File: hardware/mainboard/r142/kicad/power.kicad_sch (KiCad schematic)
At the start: 44 parts, among them J1 1S LiPo PCM / PH-2, J8 External cell NTC / hand sold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, Q2 AO3401A, SW1 MK-12C03-G015, U3 BQ24072TRGTR, U4 TPS63802DLAR

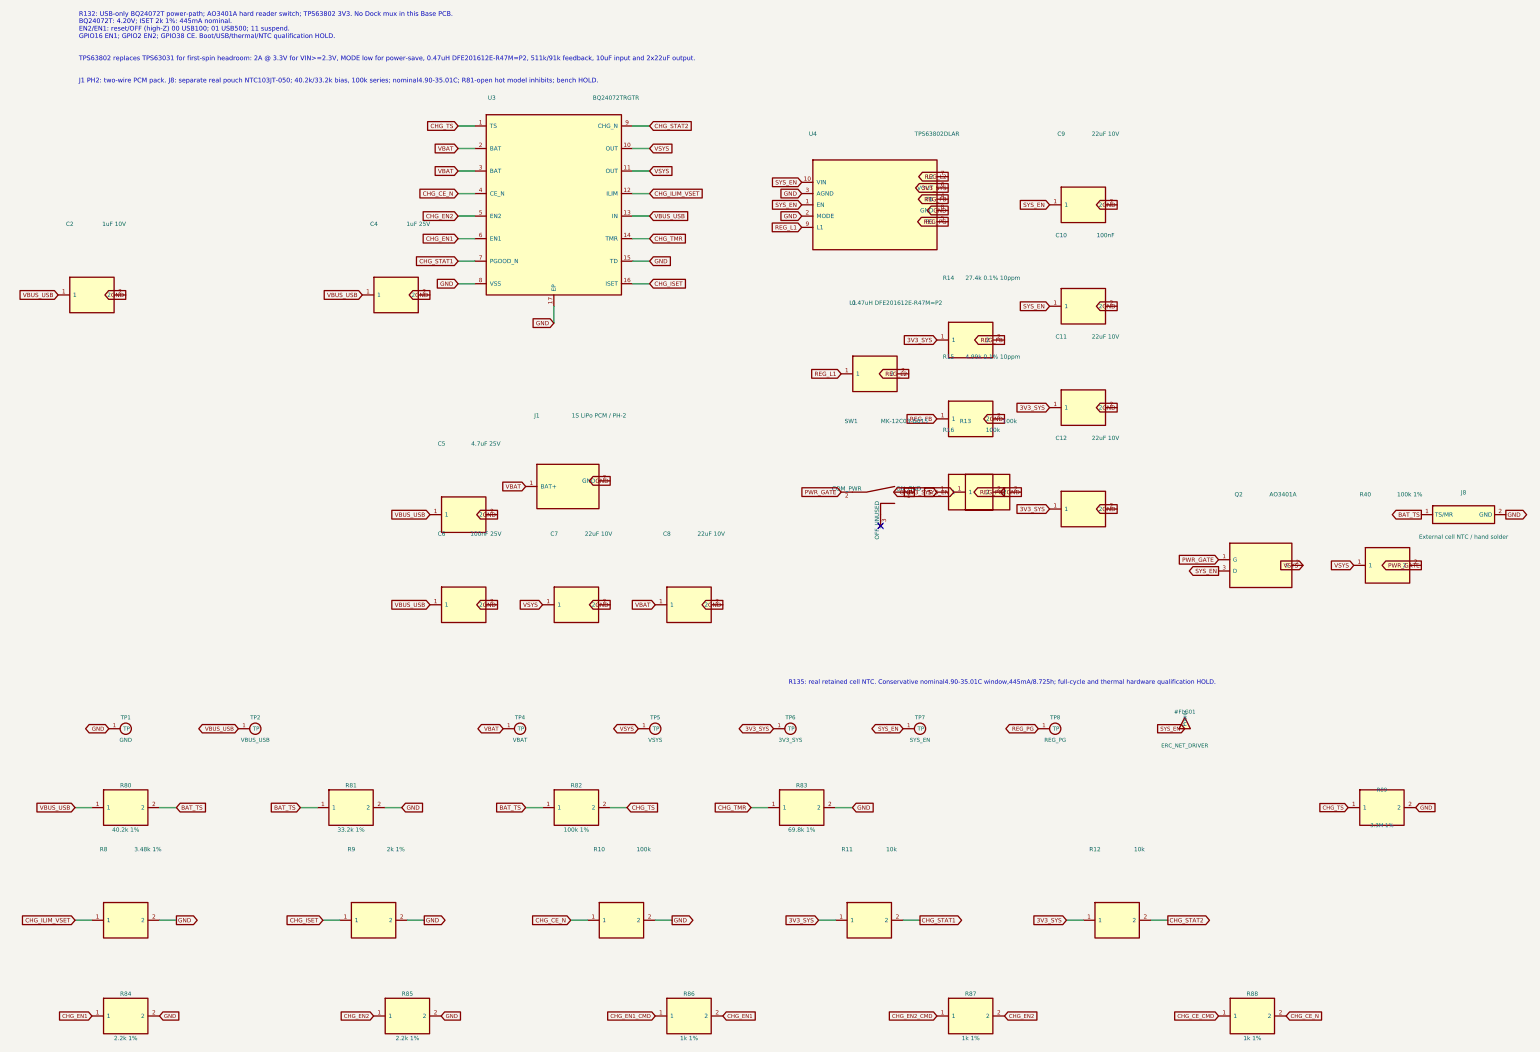
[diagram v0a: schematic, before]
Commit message: R142: separate SD schematic group and refresh engineering notes; preserve electrical graph
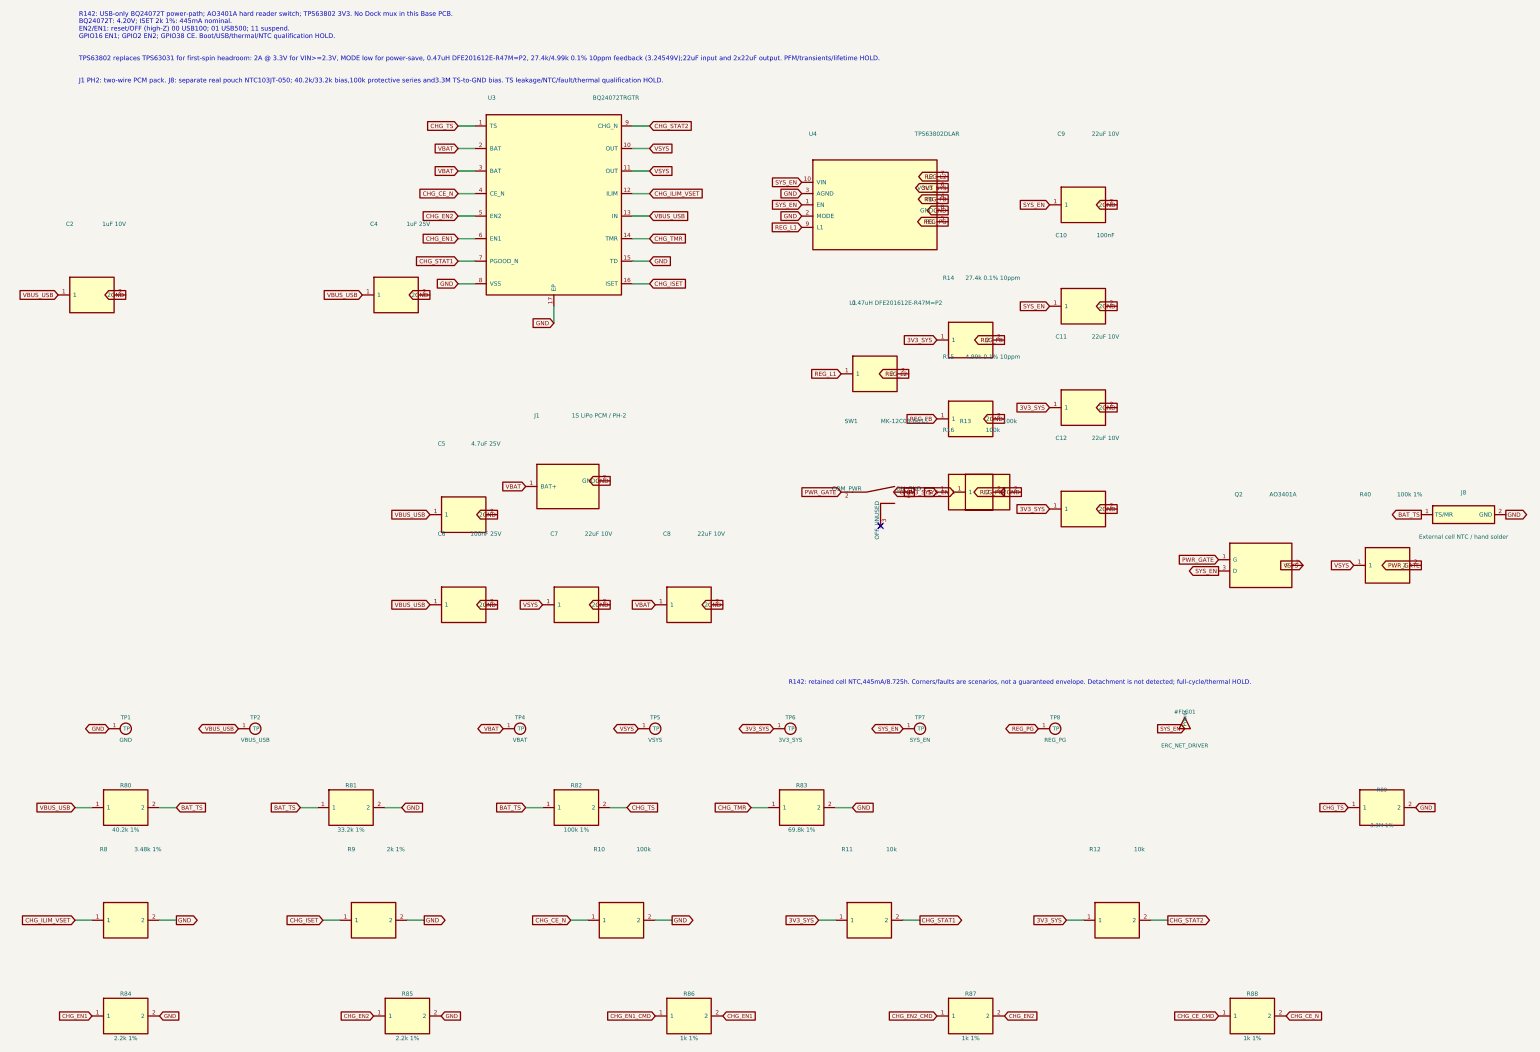
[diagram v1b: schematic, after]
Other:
- note added: "J1 PH2: two-wire PCM pack. J8: separate real pouch NTC103JT-050; 40.2k/33.2k bias,100k protective series and3.3M TS-to-GND bias. TS leakage/NTC/fault/thermal qualification HOLD."
- note added: "R142: USB-only BQ24072T power-path; AO3401A hard reader switch; TPS63802 3V3. No Dock mux in this Base PCB."
- note added: "R142: retained cell NTC,445mA/8.725h. Corners/faults are scenarios, not a guaranteed envelope. Detachment is not detected; full-cycle/thermal HOLD."
- note added: "TPS63802 replaces TPS63031 for first-spin headroom: 2A @ 3.3V for VIN>=2.3V, MODE low for power-save, 0.47uH DFE201612E-R47M=P2, 27.4k/4.99k 0.1% 10ppm feedback (3.24549V);22uF input and 2x22uF output. PFM/transients/lifetime HOLD."
- note removed: "J1 PH2: two-wire PCM pack. J8: separate real pouch NTC103JT-050; 40.2k/33.2k bias, 100k series; nominal4.90-35.01C; R81-open hot model inhibits; bench HOLD."
- note removed: "R132: USB-only BQ24072T power-path; AO3401A hard reader switch; TPS63802 3V3. No Dock mux in this Base PCB."
- note removed: "R135: real retained cell NTC. Conservative nominal4.90-35.01C window,445mA/8.725h; full-cycle and thermal hardware qualification HOLD."
- note removed: "TPS63802 replaces TPS63031 for first-spin headroom: 2A @ 3.3V for VIN>=2.3V, MODE low for power-save, 0.47uH DFE201612E-R47M=P2, 511k/91k feedback, 10uF input and 2x22uF output."
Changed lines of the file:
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@@
 	(global_label "3V3_SYS" (shape input) (at 218.44 127 0) (effects (font (size 0.95 0.95)) (justify right bottom)))
 	(global_label "REG_PG" (shape output) (at 233.68 127 180) (effects (font (size 0.95 0.95)) (justify right bottom)))
-	(text "R132: USB-only BQ24072T power-path; AO3401A hard reader switch; TPS63802 3V3. No Dock mux in this Base PCB." (exclude_from_sim no) (at 25 20 0) (effects (font (size 1.05 1.05)) (justify left bottom)))
+	(text "R142: USB-only BQ24072T power-path; AO3401A hard reader switch; TPS63802 3V3. No Dock mux in this Base PCB." (exclude_from_sim no) (at 25 20 0) (effects (font (size 1.05 1.05)) (justify left bottom)))
 	(text "BQ24072T: 4.20V; ISET 2k 1%: 445mA nominal.\nEN2/EN1: reset/OFF (high-Z) 00 USB100; 01 USB500; 11 suspend.\nGPIO16 EN1; GPIO2 EN2; GPIO38 CE. Boot/USB/thermal/NTC qualification HOLD." (exclude_from_sim no) (at 25 25 0) (effects (font (size 1.05 1.05)) (justify left bottom)))
-	(text "TPS63802 replaces TPS63031 for first-spin headroom: 2A @ 3.3V for VIN>=2.3V, MODE low for power-save, 0.47uH DFE201612E-R47M=P2, 511k/91k feedback, 10uF input and 2x22uF output." (exclude_from_sim no) (at 25 30 0) (effects (font (size 1.05 1.05)) (justify left bottom)))
-	(text "J1 PH2: two-wire PCM pack. J8: separate real pouch NTC103JT-050; 40.2k/33.2k bias, 100k series; nominal4.90-35.01C; R81-open hot model inhibits; bench HOLD." (exclude_from_sim no) (at 25 35 0) (effects (font (size 1.05 1.05)) (justify left bottom)))
+	(text "TPS63802 replaces TPS63031 for first-spin headroom: 2A @ 3.3V for VIN>=2.3V, MODE low for power-save, 0.47uH DFE201612E-R47M=P2, 27.4k/4.99k 0.1% 10ppm feedback (3.24549V);22uF input and 2x22uF output. PFM/transients/lifetime HOLD." (exclude_from_sim no) (at 25 30 0) (effects (font (size 1.05 1.05)) (justify left bottom)))
+	(text "J1 PH2: two-wire PCM pack. J8: separate real pouch NTC103JT-050; 40.2k/33.2k bias,100k protective series and3.3M TS-to-GND bias. TS leakage/NTC/fault/thermal qualification HOLD." (exclude_from_sim no) (at 25 35 0) (effects (font (size 1.05 1.05)) (justify left bottom)))
 	(symbol (lib_id "ENKU:TESTPOINT") (at 35.56 180.34 0) (unit 1) (exclude_from_sim no) (in_bom no) (on_board yes) (dnp no)
 		(property "Reference" "TP1" (at 35.56 177.8 0) (effects (font (size 0.9 0.9))))
@@
    (global_label "BAT_TS" (shape output) (at 327.66 132.08 0) (effects (font (size .95 .95)) (justify right bottom)))
    (global_label "GND" (shape output) (at 346.71 132.08 180) (effects (font (size .95 .95)) (justify left bottom)))
-   (text "R135: real retained cell NTC. Conservative nominal4.90-35.01C window,445mA/8.725h; full-cycle and thermal hardware qualification HOLD." (at 185 170 0) (effects (font (size 1 1)) (justify left)))
+   (text "R142: retained cell NTC,445mA/8.725h. Corners/faults are scenarios, not a guaranteed envelope. Detachment is not detected; full-cycle/thermal HOLD." (at 185 170 0) (effects (font (size 1 1)) (justify left)))
 (global_label "CHG_TS" (shape input) (at 110.49 44.45 0) (effects (font (size .95 .95)) (justify right bottom)))
 (global_label "VBAT" (shape input) (at 110.49 49.53 0) (effects (font (size .95 .95)) (justify right bottom)))
